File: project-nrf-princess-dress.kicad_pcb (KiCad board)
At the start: 2 copper layers, 58 x 65 mm, 28 parts, among them J1 Conn_01x02_Female, J2 Conn_01x04_Female, J3 Conn_01x12_Female, J4 Conn_01x04_Female, J5 Conn_01x12_Female, J6 Conn_01x01_Female, J7 Conn_01x04_Female, J8 SM04B-SRSS-TB(LF)(SN), Q1 Q_PMOS_GSD, U1 TXU0204BQAR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

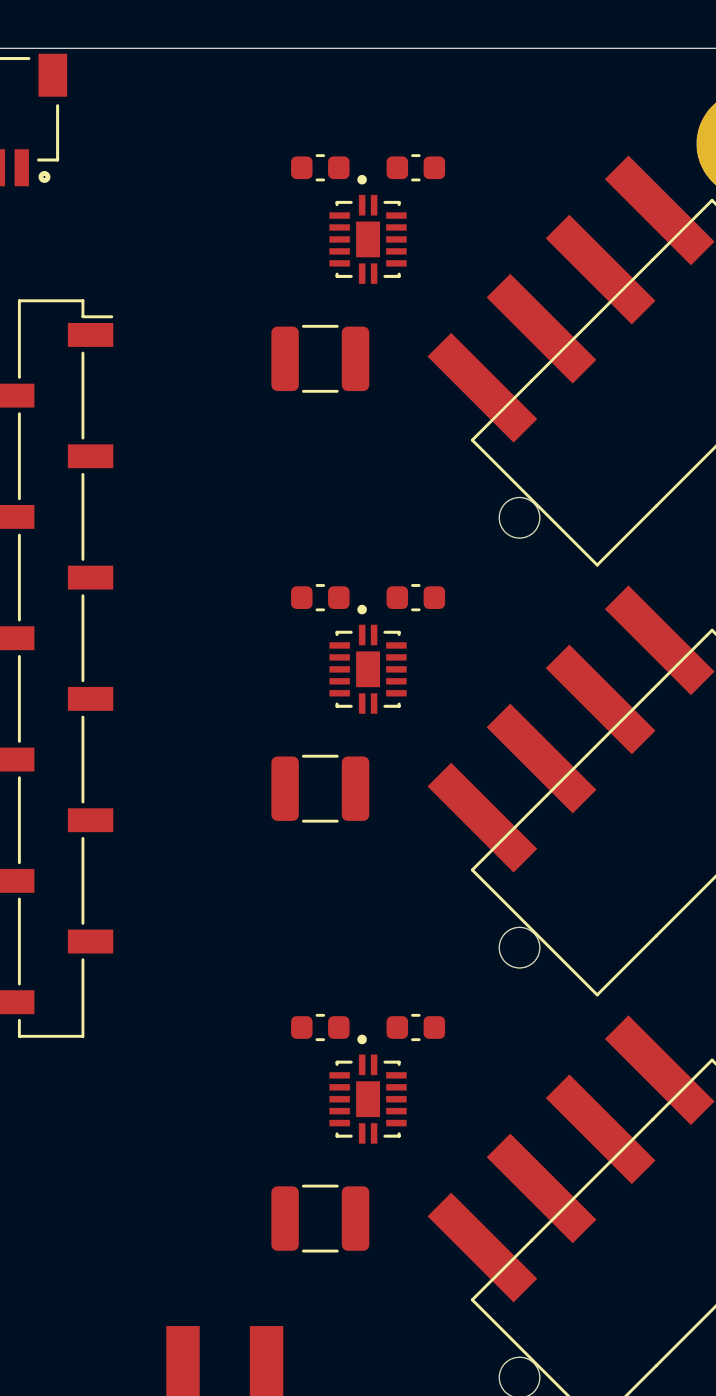
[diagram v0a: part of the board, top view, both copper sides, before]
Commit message: Move the voltage translator blocks up
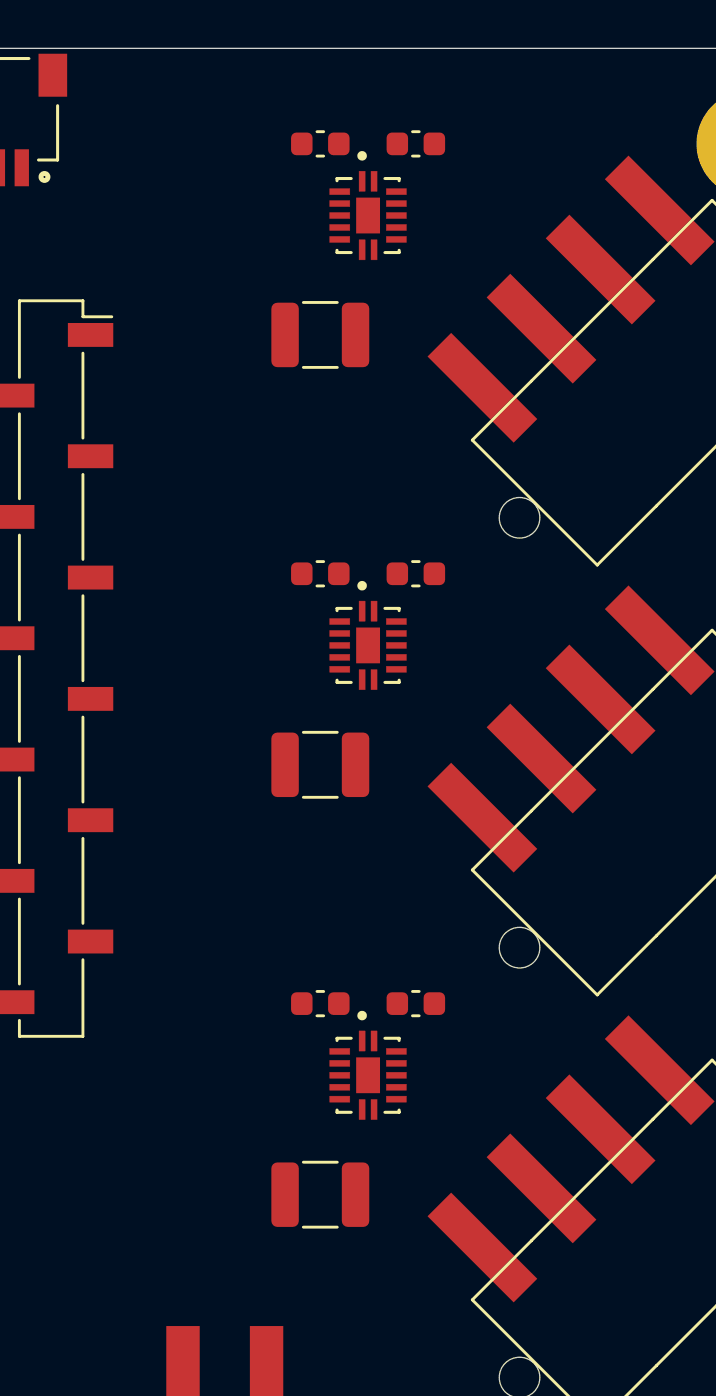
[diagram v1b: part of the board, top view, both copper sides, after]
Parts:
- moved C1 1.00 mm to (81.1, 28.8)
- moved C2 1.00 mm to (85.1, 28.8)
- moved C3 1.00 mm to (81.1, 36.8)
- moved C4 1.00 mm to (81.1, 46.8)
- moved C5 1.00 mm to (85.1, 46.8)
- moved C6 1.00 mm to (81.1, 54.8)
- moved C7 1.00 mm to (81.1, 64.8)
- moved C8 1.00 mm to (85.1, 64.8)
- moved C9 1.00 mm to (81.1, 72.8)
- moved U1 1.00 mm to (83.1, 31.8)
- moved U2 1.00 mm to (83.1, 49.8)
- moved U3 1.00 mm to (83.1, 67.8)
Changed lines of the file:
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@@
   )
   (module TXU0204BQAR:TXU0204BQAR (layer F.Cu)
-    (at 83.12 68.79)
+    (at 83.12 67.79)
     (fp_text reference U3 (at 0.765 -3.75) (layer F.Fab)
       (effects (font (size 1 1) (thickness 0.15)))
@@
   )
   (module TXU0204BQAR:TXU0204BQAR (layer F.Cu)
-    (at 83.12 50.79)
+    (at 83.12 49.79)
     (fp_text reference U2 (at 0.765 -3.75) (layer F.Fab)
       (effects (font (size 1 1) (thickness 0.15)))
@@
   )
   (module TXU0204BQAR:TXU0204BQAR (layer F.Cu)
-    (at 83.12 32.79)
+    (at 83.12 31.79)
     (fp_text reference U1 (at 0.765 -3.75) (layer F.Fab)
       (effects (font (size 1 1) (thickness 0.15)))
@@
   )
   (module Capacitor_SMD:C_1210_3225Metric (layer F.Cu)
-    (at 81.12 73.79 180)
+    (at 81.12 72.79 180)
     (descr "Capacitor SMD 1210 (3225 Metric), square (rectangular) end terminal, IPC_7351 nominal, (Body size source: IPC-SM-782 page 76, https://www.pcb-3d.com/wordpress/wp-content/uploads/ipc-sm-782a_amendment_1_and_2.pdf), generated with kicad-footprint-generator")
     (tags capacitor)
@@
   )
   (module Capacitor_SMD:C_0603_1608Metric (layer F.Cu)
-    (at 85.12 65.79)
+    (at 85.12 64.79)
     (descr "Capacitor SMD 0603 (1608 Metric), square (rectangular) end terminal, IPC_7351 nominal, (Body size source: IPC-SM-782 page 76, https://www.pcb-3d.com/wordpress/wp-content/uploads/ipc-sm-782a_amendment_1_and_2.pdf), generated with kicad-footprint-generator")
     (tags capacitor)
@@
   )
   (module Capacitor_SMD:C_0603_1608Metric (layer F.Cu)
-    (at 81.12 65.79 180)
+    (at 81.12 64.79 180)
     (descr "Capacitor SMD 0603 (1608 Metric), square (rectangular) end terminal, IPC_7351 nominal, (Body size source: IPC-SM-782 page 76, https://www.pcb-3d.com/wordpress/wp-content/uploads/ipc-sm-782a_amendment_1_and_2.pdf), generated with kicad-footprint-generator")
     (tags capacitor)
@@
   )
   (module Capacitor_SMD:C_1210_3225Metric (layer F.Cu)
-    (at 81.12 55.79 180)
+    (at 81.12 54.79 180)
     (descr "Capacitor SMD 1210 (3225 Metric), square (rectangular) end terminal, IPC_7351 nominal, (Body size source: IPC-SM-782 page 76, https://www.pcb-3d.com/wordpress/wp-content/uploads/ipc-sm-782a_amendment_1_and_2.pdf), generated with kicad-footprint-generator")
     (tags capacitor)
@@
   )
   (module Capacitor_SMD:C_0603_1608Metric (layer F.Cu)
-    (at 85.12 47.79)
+    (at 85.12 46.79)
     (descr "Capacitor SMD 0603 (1608 Metric), square (rectangular) end terminal, IPC_7351 nominal, (Body size source: IPC-SM-782 page 76, https://www.pcb-3d.com/wordpress/wp-content/uploads/ipc-sm-782a_amendment_1_and_2.pdf), generated with kicad-footprint-generator")
     (tags capacitor)
@@
   )
   (module Capacitor_SMD:C_0603_1608Metric (layer F.Cu)
-    (at 81.12 47.79)
+    (at 81.12 46.79)
     (descr "Capacitor SMD 0603 (1608 Metric), square (rectangular) end terminal, IPC_7351 nominal, (Body size source: IPC-SM-782 page 76, https://www.pcb-3d.com/wordpress/wp-content/uploads/ipc-sm-782a_amendment_1_and_2.pdf), generated with kicad-footprint-generator")
     (tags capacitor)
@@
   )
   (module Capacitor_SMD:C_1210_3225Metric (layer F.Cu)
-    (at 81.12 37.79 180)
+    (at 81.12 36.79 180)
     (descr "Capacitor SMD 1210 (3225 Metric), square (rectangular) end terminal, IPC_7351 nominal, (Body size source: IPC-SM-782 page 76, https://www.pcb-3d.com/wordpress/wp-content/uploads/ipc-sm-782a_amendment_1_and_2.pdf), generated with kicad-footprint-generator")
     (tags capacitor)
@@
   )
   (module Capacitor_SMD:C_0603_1608Metric (layer F.Cu)
-    (at 85.12 29.79)
+    (at 85.12 28.79)
     (descr "Capacitor SMD 0603 (1608 Metric), square (rectangular) end terminal, IPC_7351 nominal, (Body size source: IPC-SM-782 page 76, https://www.pcb-3d.com/wordpress/wp-content/uploads/ipc-sm-782a_amendment_1_and_2.pdf), generated with kicad-footprint-generator")
     (tags capacitor)
@@
   )
   (module Capacitor_SMD:C_0603_1608Metric (layer F.Cu)
-    (at 81.12 29.79 180)
+    (at 81.12 28.79 180)
     (descr "Capacitor SMD 0603 (1608 Metric), square (rectangular) end terminal, IPC_7351 nominal, (Body size source: IPC-SM-782 page 76, https://www.pcb-3d.com/wordpress/wp-content/uploads/ipc-sm-782a_amendment_1_and_2.pdf), generated with kicad-footprint-generator")
     (tags capacitor)

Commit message: Change i2c pins order
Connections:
- J6 pad 1: /P0.22 -> /P0.09
- J8 pad 3: /P0.09 -> /P0.22
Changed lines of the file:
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@@
     )
     (pad 1 smd rect (at 0 0 180) (size 3 5) (layers F.Cu F.Paste F.Mask)
-      (net 16 /P0.22))
+      (net 12 /P0.09))
   )
   (module TXU0204BQAR:TXU0204BQAR (layer F.Cu)
@@
       (net 17 /P0.10))
     (pad 3 smd rect (at 0.5 0 180) (size 0.6 1.55) (layers F.Cu F.Paste F.Mask)
-      (net 12 /P0.09))
+      (net 16 /P0.22))
     (pad 2 smd rect (at -0.5 0 180) (size 0.6 1.55) (layers F.Cu F.Paste F.Mask)
       (net 2 VDD))

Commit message: Routing
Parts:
- moved Q1 1.00 mm to (92.1, 85.8)
- moved R1 1.00 mm to (86.1, 85.8)
- moved R2 1.00 mm to (89.1, 85.8)
- turned C4 to 180 degrees
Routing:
- net GND: track 0.00 -> 29.0 mm, vias 0 -> 17
- net /P0.02: track 0.00 -> 26.3 mm
- net /P1.15: track 0.00 -> 25.2 mm
- net /P1.14: track 0.00 -> 17.1 mm
- net /P1.03: track 0.00 -> 15.8 mm
- net /P0.03: track 0.00 -> 13.3 mm
- net /P1.10: track 0.00 -> 12.9 mm
- net Net-(J4-Pad3): track 0.00 -> 9.90 mm
- net Net-(J2-Pad3): track 0.00 -> 9.90 mm
- net Net-(J7-Pad3): track 0.00 -> 9.90 mm
- net Net-(J4-Pad2): track 0.00 -> 8.25 mm
- net Net-(J2-Pad2): track 0.00 -> 8.25 mm
- net Net-(J7-Pad2): track 0.00 -> 8.25 mm
- net VDD: track 0.00 -> 4.13 mm
- net +BATT: track 0.00 -> 4.13 mm
- added copper zone on B.Cu, net GND

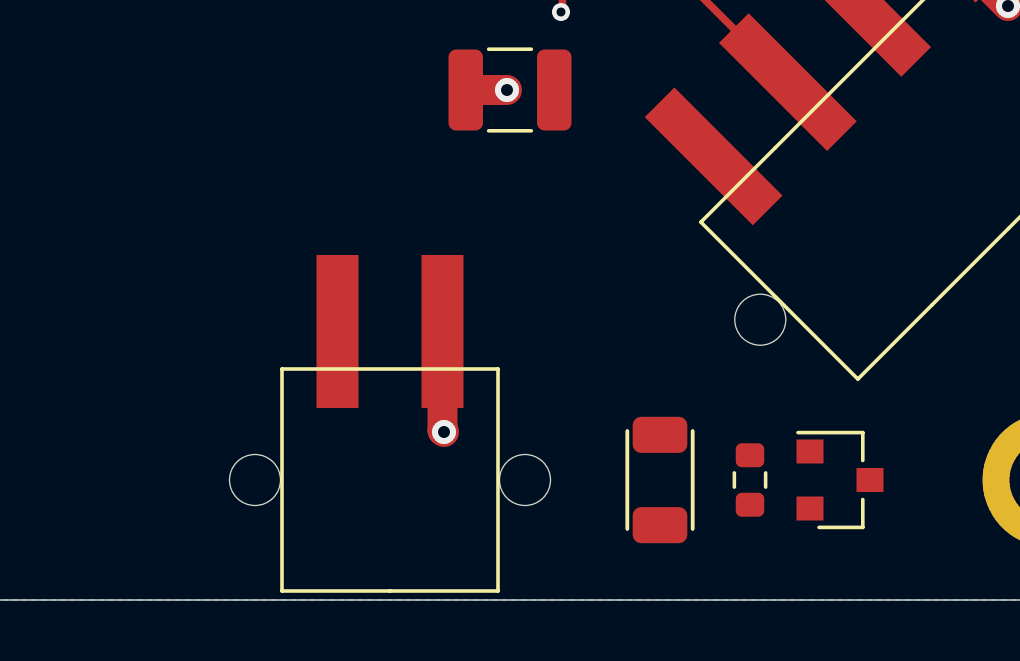
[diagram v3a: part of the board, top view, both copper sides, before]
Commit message: Add power input planes
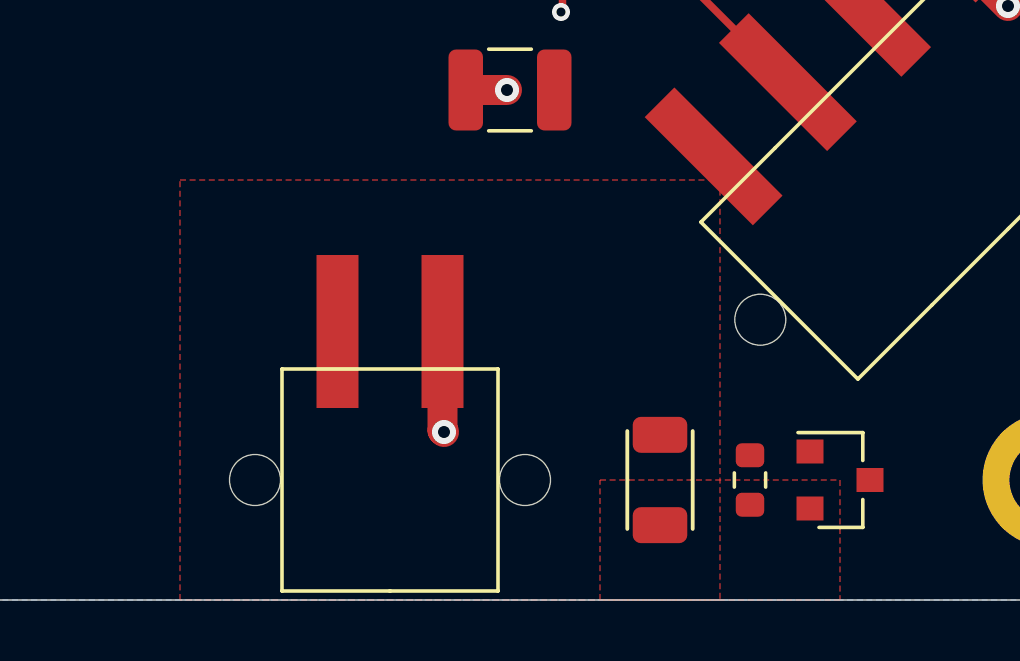
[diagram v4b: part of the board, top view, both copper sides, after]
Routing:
- added copper zone on F.Cu, net Net-(J1-Pad1)
- added copper zone on F.Cu, net Net-(Q1-Pad2)
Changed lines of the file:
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@@
+    )
+  )
+  (zone (net 32) (net_name "Net-(Q1-Pad2)") (layer F.Cu) (hatch edge 0.508)
+    (priority 2)
+    (connect_pads (clearance 0.508))
+    (min_thickness 0.254)
+    (fill yes (arc_segments 32) (thermal_gap 0.508) (thermal_bridge_width 0.508) (smoothing fillet) (radius 0.5))
+    (polygon
+      (pts
+        (xy 92.12 89.79) (xy 84.12 89.79) (xy 84.12 85.79) (xy 92.12 85.79)
+      )
+    )
+  )
+  (zone (net 4) (net_name "Net-(J1-Pad1)") (layer F.Cu) (hatch edge 0.508)
+    (priority 1)
+    (connect_pads (clearance 0.508))
+    (min_thickness 0.254)
+    (fill yes (arc_segments 32) (thermal_gap 0.508) (thermal_bridge_width 0.508) (smoothing fillet) (radius 0.5))
+    (polygon
+      (pts
+        (xy 88.12 89.79) (xy 70.12 89.79) (xy 70.12 75.79) (xy 88.12 75.79)
+      )
     )
   )

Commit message: Routing done
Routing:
- net Net-(Q1-Pad1): track 0.00 -> 37.1 mm, vias 0 -> 2
- net +BATT: track 4.13 -> 33.8 mm, vias 0 -> 2
- net /P0.22: track 0.00 -> 26.6 mm
- net /P0.10: track 0.00 -> 22.7 mm
- net /P0.09: track 0.00 -> 15.2 mm
- net VDD: track 4.13 -> 15.5 mm
- net GND: track 29.0 -> 33.6 mm, vias 17 -> 21
- added copper zone on F.Cu, net +BATT
- added copper zone on F.Cu, net VDD
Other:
- outline, holes or cut-outs redrawn

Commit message: Add silk
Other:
- board text added: "+"
- board text added: "GND"
- board text added: "INT"
- board text added: "Julie Gervais François Gervais 5 dec 2022 v"
- board text added: "ON"
- board text added: "StemmaQT"
- board text added: "VBATT"
- board text added: "VDD"
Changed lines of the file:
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@@
   (general
     (thickness 1.6)
-    (drawings 17)
+    (drawings 27)
     (tracks 145)
     (zones 0)
@@
     )
   )
+  (gr_text StemmaQT (at 67.12 31.79) (layer F.SilkS)
+    (effects (font (size 1 1) (thickness 0.15)))
+  )
+  (gr_text INT (at 57.62 27.79 90) (layer F.SilkS)
+    (effects (font (size 1 1) (thickness 0.15)))
+  )
+  (gr_text VBATT (at 64.62 59.79) (layer F.SilkS)
+    (effects (font (size 1 1) (thickness 0.15)))
+  )
+  (gr_text GND (at 52.62 67.29) (layer F.SilkS)
+    (effects (font (size 1 1) (thickness 0.15)))
+  )
+  (gr_text VDD (at 65.12 64.79) (layer F.SilkS)
+    (effects (font (size 1 1) (thickness 0.15)))
+  )
+  (gr_text + (at 73.12 79.79) (layer F.SilkS)
+    (effects (font (size 1 1) (thickness 0.15)))
+  )
+  (gr_text GND (at 91.62 28.79) (layer F.SilkS)
+    (effects (font (size 1 1) (thickness 0.15)))
+  )
+  (gr_text VBATT (at 84.12 40.29) (layer F.SilkS)
+    (effects (font (size 1 1) (thickness 0.15)))
+  )
+  (gr_text "Julie Gervais\nFrançois Gervais\n5 dec 2022\nv" (at 61.12 79.29) (layer B.SilkS)
+    (effects (font (size 1 1) (thickness 0.15)) (justify left mirror))
+  )
+  (gr_text ON (at 52.62 85.79 90) (layer F.SilkS)
+    (effects (font (size 1 1) (thickness 0.15)))
+  )
   (gr_arc (start 99.12 28.79) (end 103.12 28.79) (angle -90) (layer Edge.Cuts) (width 0.05))

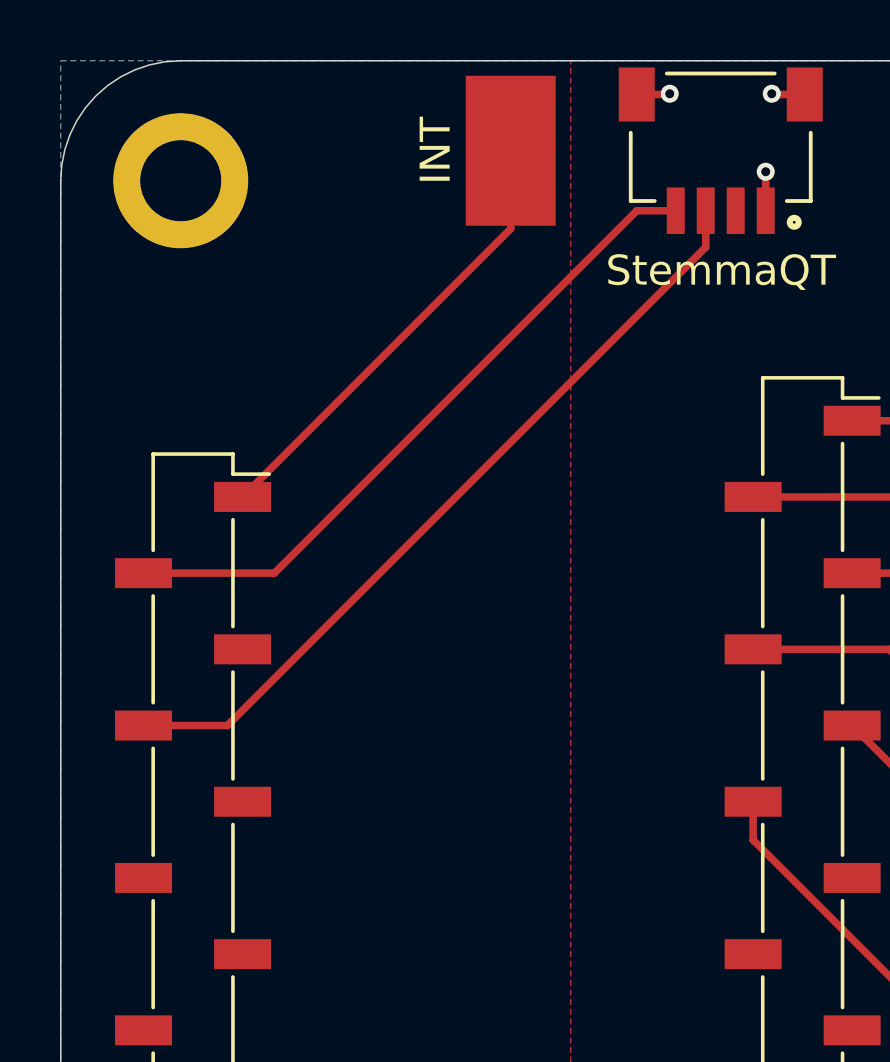
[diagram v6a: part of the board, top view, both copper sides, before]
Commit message: Add a pad for the ism330dhcx int2
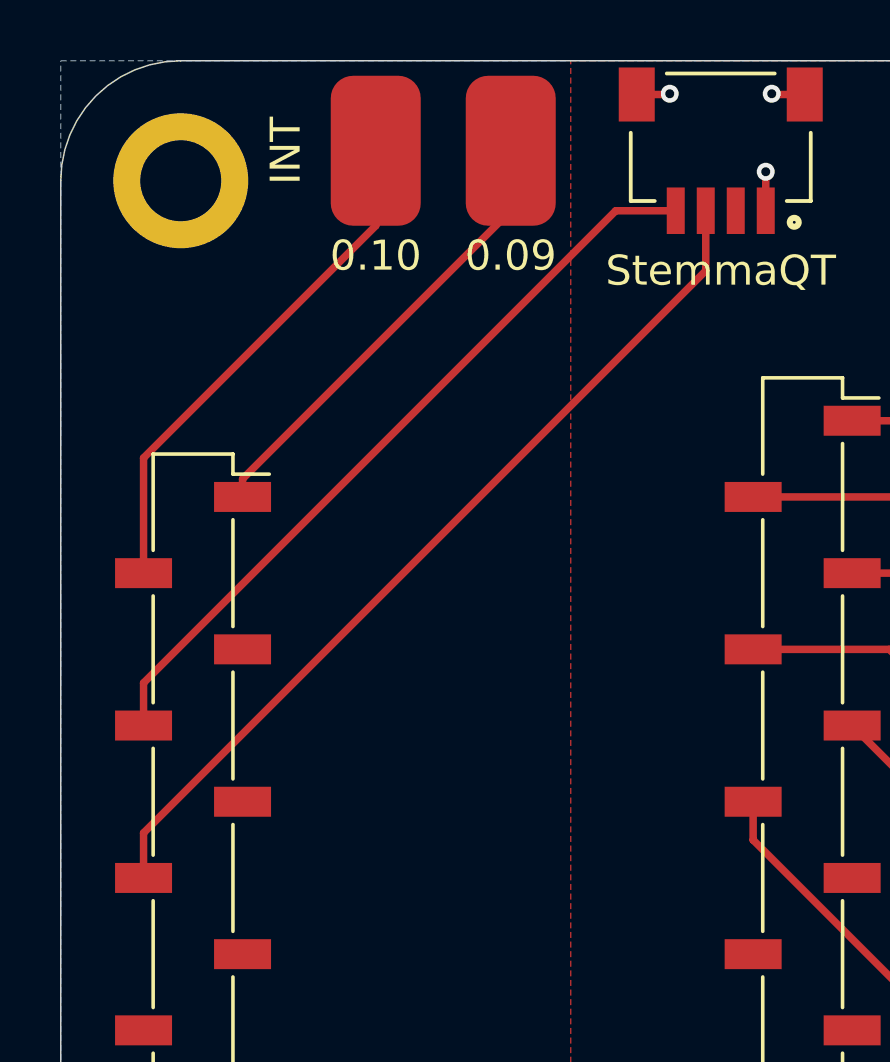
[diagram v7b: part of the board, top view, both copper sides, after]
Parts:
- added J9: Conn_01x01_Female, Connector_Wire:SolderWirePad_1x01_SMD_5x10mm, F.Cu at (55.6, 27.8)
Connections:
- J8 pad 3: /P0.22 -> /P0.23
- J8 pad 4: /P0.10 -> /P0.22
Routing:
- net /P0.23: track 0.00 -> 30.0 mm
- net /P0.10: track 22.7 -> 17.3 mm
- net /P0.22: track 26.6 -> 25.7 mm
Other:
- board text added: "0.09"
- board text added: "0.10"

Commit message: Change the PMOS value
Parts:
- Q1: value Q_PMOS_GSD -> SI2301CDS-T1-E3
